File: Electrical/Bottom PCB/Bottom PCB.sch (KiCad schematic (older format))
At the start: 41 parts, among them J101 Steper1, J102 Steper2, J103 H Bridge, J104 Servo1, J105 Servo2, J106 Servo3, J107 Servo4, SW101 FL, SW102 FR, U101 ULN2003A, U102 74HC595, U103 QRE1113, U104 TB6612FNG, U105 74HC595, U106 QRE1113, U107 QRE1113, U108 MCP23017_SO, U109 QRE1113

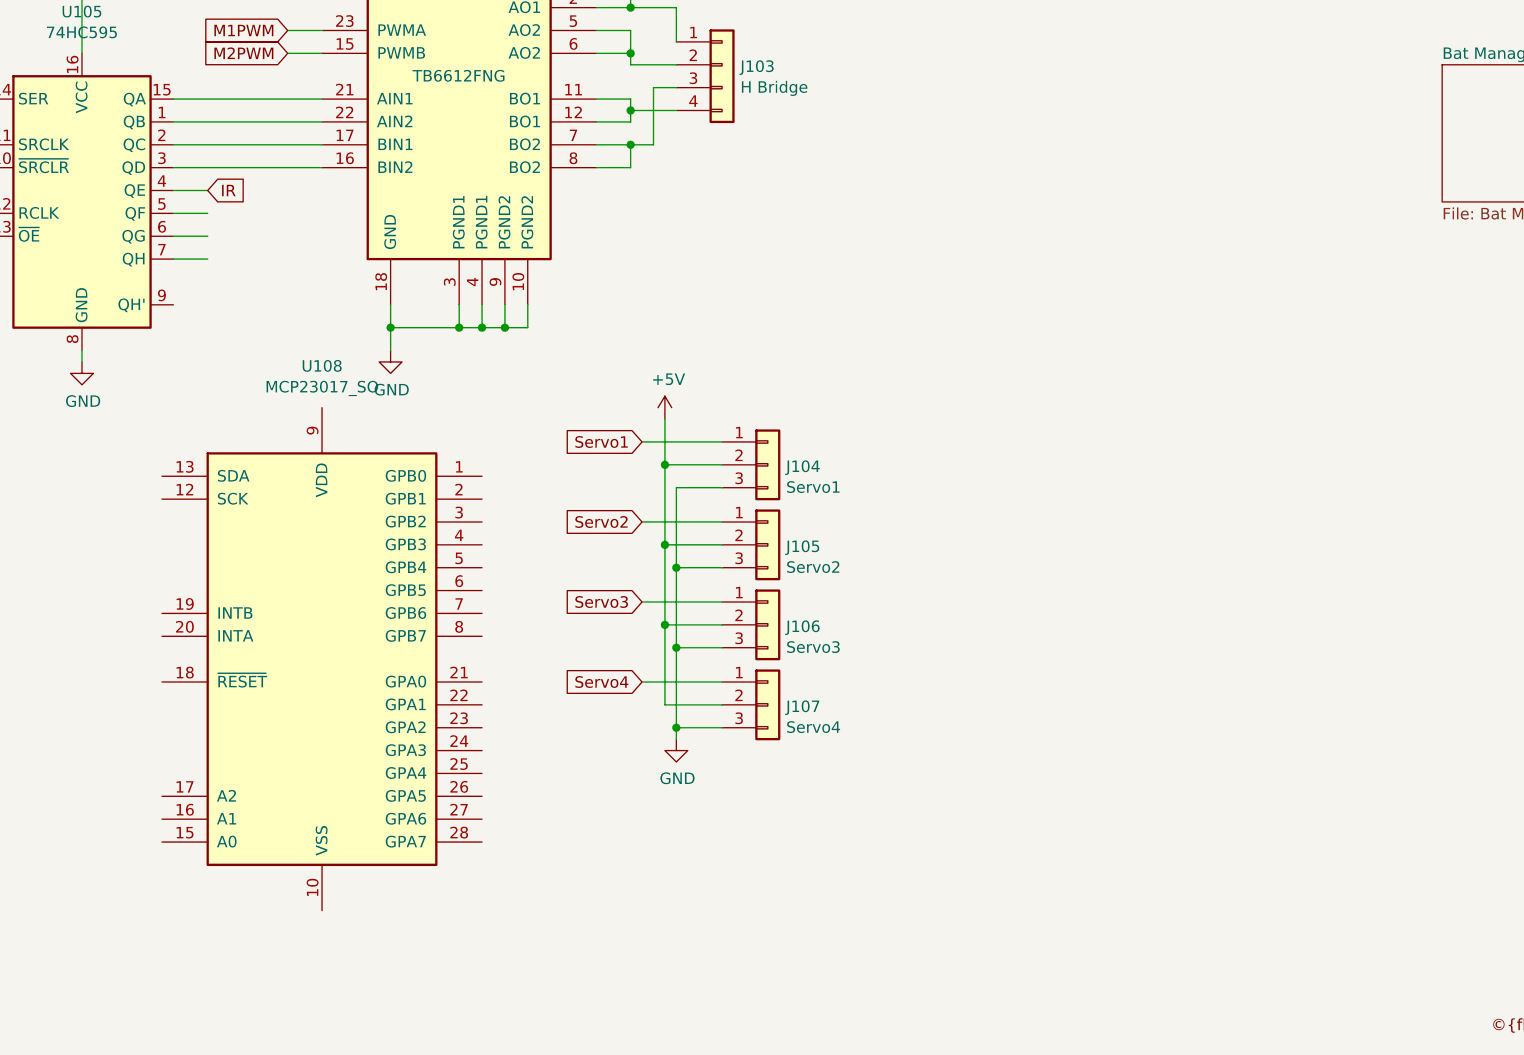
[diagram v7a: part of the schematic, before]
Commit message: Set up MCP23017
Added the main parts of an MCP23017
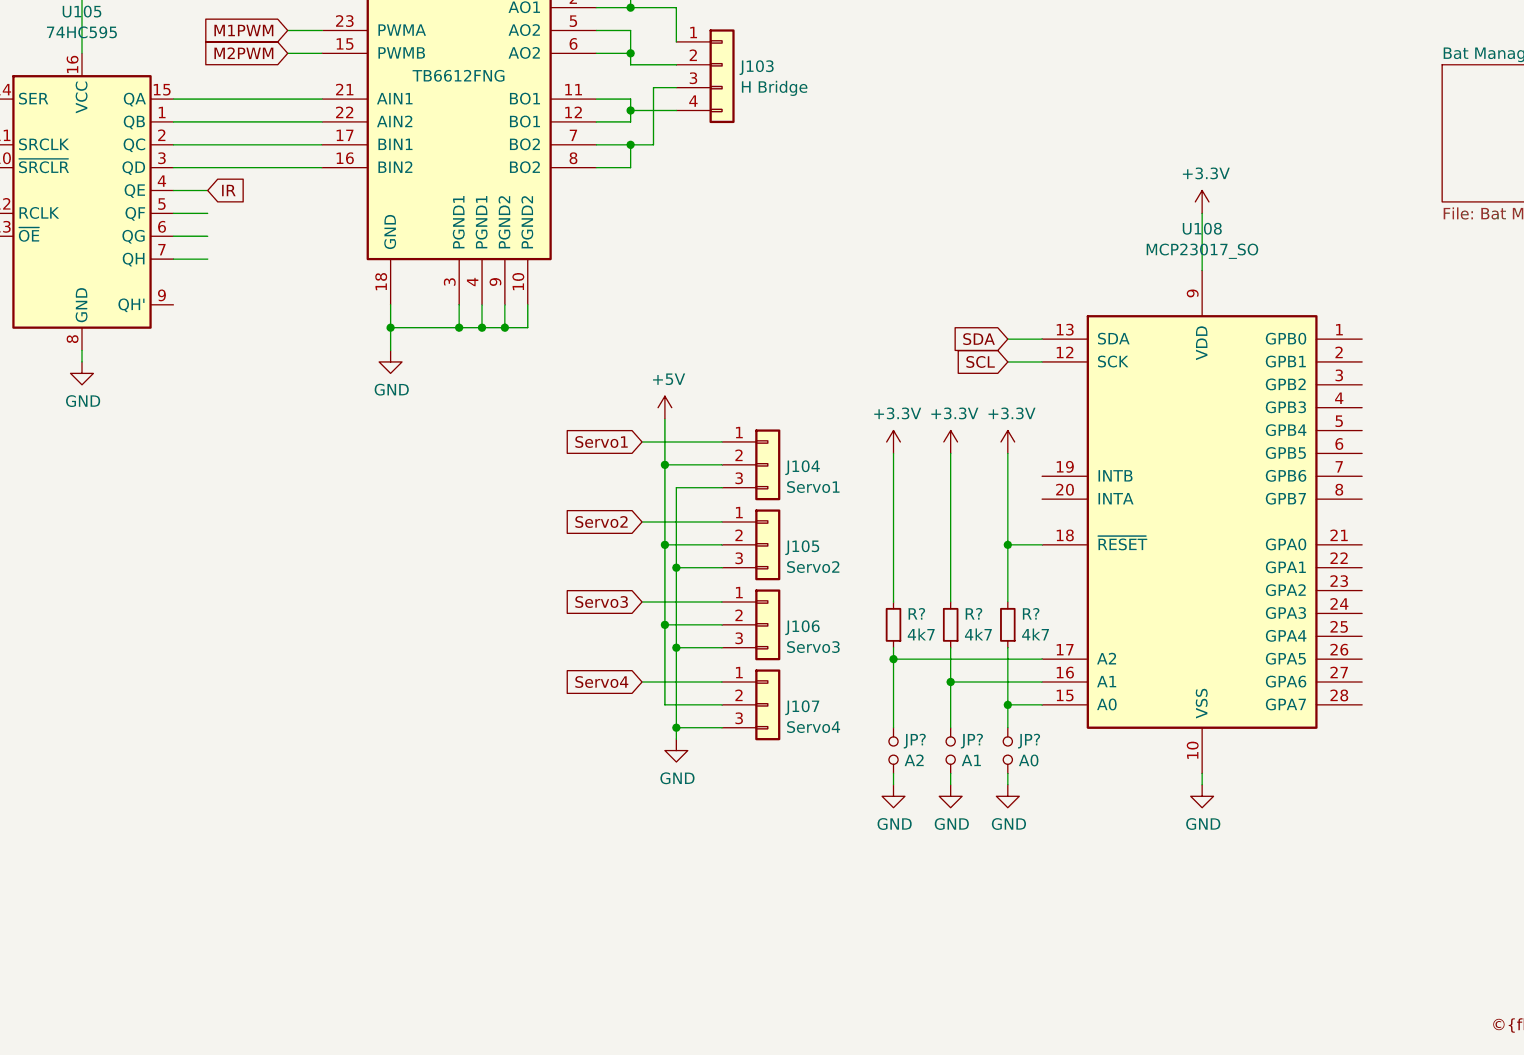
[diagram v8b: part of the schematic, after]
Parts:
- added JP?: A2, symbol Device:Jumper_NO_Small
- added JP?: A1, symbol Device:Jumper_NO_Small
- added JP?: A0, symbol Device:Jumper_NO_Small
- added R? (x3): 4k7, Resistor_SMD:R_1206_3216Metric_Pad1.42x1.75mm_HandSolder, symbol Device:R_Small
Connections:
- net GND: now also U108.10 (VSS), JP?.2, JP?.2, JP?.2
- net SCL: now reaches U108.12 (SCK)
- net SDA: now reaches U108.13 (SDA)
- net at U108.15 (A0): now also JP?.1, R?.1
- net at U108.16 (A1): now also JP?.1, R?.1
- net at U108.17 (A2): now also JP?.1, R?.1
- net +3V3: now reaches U108.18 (~RESET~)
- net +3V3: now also U108.9 (VDD), R?.2, R?.2, R?.2
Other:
- moved on the sheet: U108
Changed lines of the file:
@@
 L Interface_Expansion:MCP23017_SO U108
 U 1 1 5F0E70CE
-P 5450 5950
-F 0 "U108" H 5450 7231 50  0000 C CNN
-F 1 "MCP23017_SO" H 5450 7140 50  0000 C CNN
-F 2 "Package_SO:SOIC-28W_7.5x17.9mm_P1.27mm" H 5650 4950 50  0001 L CNN
-F 3 "http://ww1.microchip.com/downloads/en/DeviceDoc/20001952C.pdf" H 5650 4850 50  0001 L CNN
-	1    5450 5950
+P 9300 5350
+F 0 "U108" H 9300 6631 50  0000 C CNN
+F 1 "MCP23017_SO" H 9300 6540 50  0000 C CNN
+F 2 "Package_SO:SOIC-28W_7.5x17.9mm_P1.27mm" H 9500 4350 50  0001 L CNN
+F 3 "http://ww1.microchip.com/downloads/en/DeviceDoc/20001952C.pdf" H 9500 4250 50  0001 L CNN
+	1    9300 5350
 	1    0    0    -1
 $EndComp
@@
 F1 "Bat Managment.sch" 50
 $EndSheet
+Wire Wire Line
+	8600 4550 8450 4550
+Wire Wire Line
+	8600 4650 8450 4650
+Text GLabel 8450 4550 0    50   Input ~ 0
+SDA
+Text GLabel 8450 4650 0    50   Input ~ 0
+SCL
+$Comp
+L power:GND #PWR?
+U 1 1 5EC22D13
+P 9300 6500
+F 0 "#PWR?" H 9300 6250 50  0001 C CNN
+F 1 "GND" H 9305 6327 50  0000 C CNN
+F 2 "" H 9300 6500 50  0001 C CNN
+F 3 "" H 9300 6500 50  0001 C CNN
+	1    9300 6500
+	1    0    0    -1
+$EndComp
+$Comp
+L power:+3.3V #PWR?
+U 1 1 5EC2D730
+P 9300 4000
+AR Path="/5EC2D730" Ref="#PWR?"  Part="1"
+AR Path="/5EBB31C5/5EC2D730" Ref="#PWR?"  Part="1"
+F 0 "#PWR?" H 9300 3850 50  0001 C CNN
+F 1 "+3.3V" H 9315 4173 50  0000 C CNN
+F 2 "" H 9300 4000 50  0001 C CNN
+F 3 "" H 9300 4000 50  0001 C CNN
+	1    9300 4000
+	1    0    0    -1
+$EndComp
+Wire Wire Line
+	9300 4250 9300 4000
+Wire Wire Line
+	9300 6500 9300 6450
+$Comp
+L power:GND #PWR?
+U 1 1 5EC63878
+P 8450 6500
+F 0 "#PWR?" H 8450 6250 50  0001 C CNN
+F 1 "GND" H 8455 6327 50  0000 C CNN
+F 2 "" H 8450 6500 50  0001 C CNN
+F 3 "" H 8450 6500 50  0001 C CNN
+	1    8450 6500
+	1    0    0    -1
+$EndComp
+Wire Wire Line
+	8600 5950 7950 5950
+Wire Wire Line
+	8600 6050 8200 6050
+Wire Wire Line
+	8600 6150 8450 6150
+$Comp
+L Device:R_Small R?
+U 1 1 5EC9C53C
+P 8450 5800
+F 0 "R?" H 8391 5754 50  0000 R CNN
+F 1 "4k7" H 8391 5845 50  0000 R CNN
+F 2 "Resistor_SMD:R_1206_3216Metric_Pad1.42x1.75mm_HandSolder" H 8450 5800 50  0001 C CNN
+F 3 "~" H 8450 5800 50  0001 C CNN
+	1    8450 5800
+	-1   0    0    1
+$EndComp
+$Comp
+L Device:R_Small R?
+U 1 1 5EC9D4EB
+P 8200 5800
+F 0 "R?" H 8141 5754 50  0000 R CNN
+F 1 "4k7" H 8141 5845 50  0000 R CNN
+F 2 "Resistor_SMD:R_1206_3216Metric_Pad1.42x1.75mm_HandSolder" H 8200 5800 50  0001 C CNN
+F 3 "~" H 8200 5800 50  0001 C CNN
+	1    8200 5800
+	-1   0    0    1
+$EndComp
+$Comp
+L Device:R_Small R?
+U 1 1 5EC9D878
+P 7950 5800
+F 0 "R?" H 7891 5754 50  0000 R CNN
+F 1 "4k7" H 7891 5845 50  0000 R CNN
+F 2 "Resistor_SMD:R_1206_3216Metric_Pad1.42x1.75mm_HandSolder" H 7950 5800 50  0001 C CNN
+F 3 "~" H 7950 5800 50  0001 C CNN
+	1    7950 5800
+	-1   0    0    1
+$EndComp
+$Comp
+L power:+3.3V #PWR?
+U 1 1 5EC9DE7B
+P 7950 5050
+AR Path="/5EC9DE7B" Ref="#PWR?"  Part="1"
+AR Path="/5EBB31C5/5EC9DE7B" Ref="#PWR?"  Part="1"
+F 0 "#PWR?" H 7950 4900 50  0001 C CNN
+F 1 "+3.3V" H 7965 5223 50  0000 C CNN
+F 2 "" H 7950 5050 50  0001 C CNN
+F 3 "" H 7950 5050 50  0001 C CNN
+	1    7950 5050
+	1    0    0    -1
+$EndComp
+$Comp
+L power:+3.3V #PWR?
+U 1 1 5EC9E5C8
+P 8200 5050
+AR Path="/5EC9E5C8" Ref="#PWR?"  Part="1"
+AR Path="/5EBB31C5/5EC9E5C8" Ref="#PWR?"  Part="1"
+F 0 "#PWR?" H 8200 4900 50  0001 C CNN
+F 1 "+3.3V" H 8215 5223 50  0000 C CNN
+F 2 "" H 8200 5050 50  0001 C CNN
+F 3 "" H 8200 5050 50  0001 C CNN
+	1    8200 5050
+	1    0    0    -1
+$EndComp
+$Comp
+L power:+3.3V #PWR?
+U 1 1 5EC9EA1E
+P 8450 5050
+AR Path="/5EC9EA1E" Ref="#PWR?"  Part="1"
+AR Path="/5EBB31C5/5EC9EA1E" Ref="#PWR?"  Part="1"
+F 0 "#PWR?" H 8450 4900 50  0001 C CNN
+F 1 "+3.3V" H 8465 5223 50  0000 C CNN
+F 2 "" H 8450 5050 50  0001 C CNN
+F 3 "" H 8450 5050 50  0001 C CNN
+	1    8450 5050
+	1    0    0    -1
+$EndComp
+$Comp
+L power:GND #PWR?
+U 1 1 5EC9EEA2
+P 8200 6500
+F 0 "#PWR?" H 8200 6250 50  0001 C CNN
+F 1 "GND" H 8205 6327 50  0000 C CNN
+F 2 "" H 8200 6500 50  0001 C CNN
+F 3 "" H 8200 6500 50  0001 C CNN
+	1    8200 6500
+	1    0    0    -1
+$EndComp
+$Comp
+L power:GND #PWR?
+U 1 1 5EC9F293
+P 7950 6500
+F 0 "#PWR?" H 7950 6250 50  0001 C CNN
+F 1 "GND" H 7955 6327 50  0000 C CNN
+F 2 "" H 7950 6500 50  0001 C CNN
+F 3 "" H 7950 6500 50  0001 C CNN
+	1    7950 6500
+	1    0    0    -1
+$EndComp
+$Comp
+L Device:Jumper_NO_Small JP?
+U 1 1 5ED31093
+P 7950 6350
+F 0 "JP?" V 7904 6398 50  0000 L CNN
+F 1 "A2" V 7995 6398 50  0000 L CNN
+F 2 "" H 7950 6350 50  0001 C CNN
+F 3 "~" H 7950 6350 50  0001 C CNN
+	1    7950 6350
+	0    1    1    0
+$EndComp
+$Comp
+L Device:Jumper_NO_Small JP?
+U 1 1 5ED31914
+P 8200 6350
+F 0 "JP?" V 8154 6398 50  0000 L CNN
+F 1 "A1" V 8245 6398 50  0000 L CNN
+F 2 "" H 8200 6350 50  0001 C CNN
+F 3 "~" H 8200 6350 50  0001 C CNN
+	1    8200 6350
+	0    1    1    0
+$EndComp
+$Comp
+L Device:Jumper_NO_Small JP?
+U 1 1 5ED31D98
+P 8450 6350
+F 0 "JP?" V 8404 6398 50  0000 L CNN
+F 1 "A0" V 8495 6398 50  0000 L CNN
+F 2 "" H 8450 6350 50  0001 C CNN
+F 3 "~" H 8450 6350 50  0001 C CNN
+	1    8450 6350
+	0    1    1    0
+$EndComp
+Wire Wire Line
+	7950 5900 7950 5950
+Wire Wire Line
+	7950 5950 7950 6250
+Connection ~ 7950 5950
+Wire Wire Line
+	8200 5900 8200 6050
+Wire Wire Line
+	8200 6050 8200 6250
+Connection ~ 8200 6050
+Wire Wire Line
+	8450 6250 8450 6150
+Wire Wire Line
+	8450 6150 8450 5900
+Connection ~ 8450 6150
+Wire Wire Line
+	8450 6500 8450 6450
+Wire Wire Line
+	8200 6500 8200 6450
+Wire Wire Line
+	7950 6500 7950 6450
+Wire Wire Line
+	8450 5050 8450 5450
+Wire Wire Line
+	8200 5050 8200 5700
+Wire Wire Line
+	7950 5050 7950 5700
+Wire Wire Line
+	8600 5450 8450 5450
+Connection ~ 8450 5450
+Wire Wire Line
+	8450 5450 8450 5700
 $EndSCHEMATC
